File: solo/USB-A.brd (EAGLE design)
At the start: 42.8 x 15 mm, 23 parts, among them U1 USB_TRACES

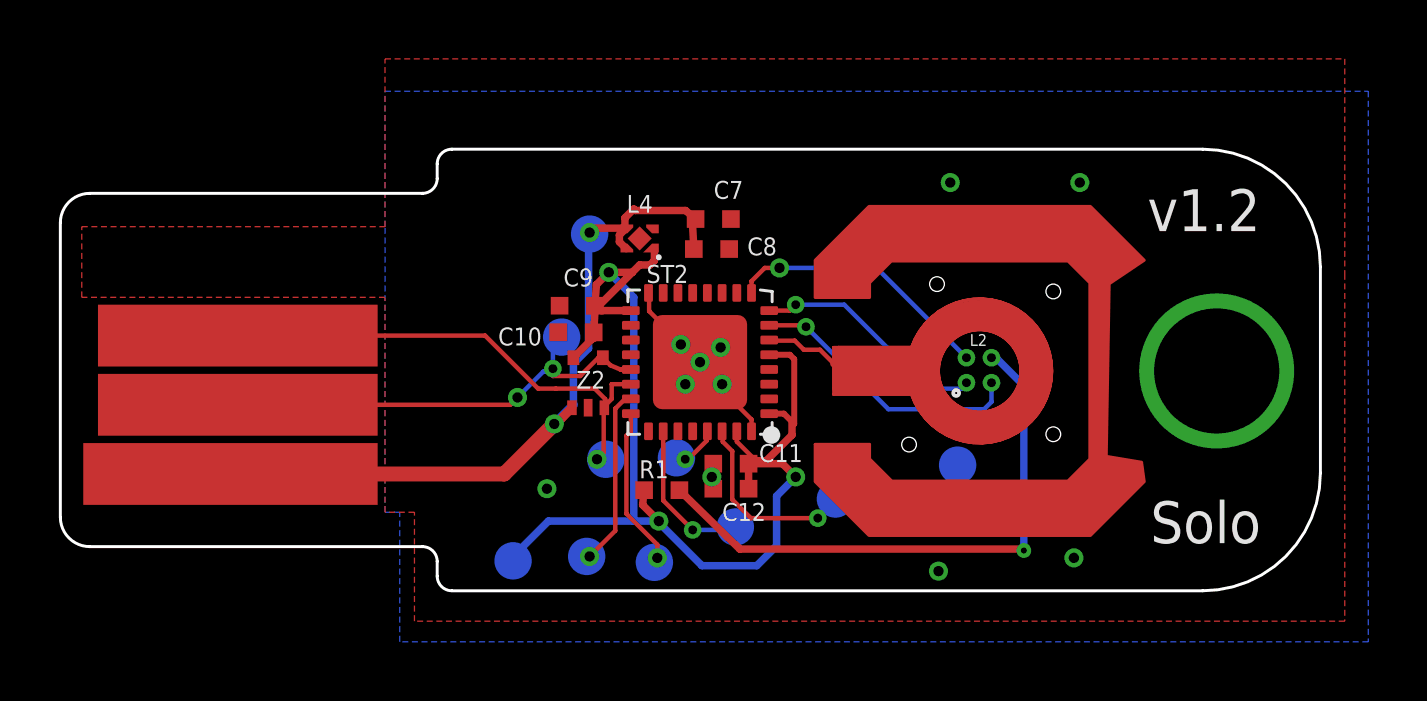
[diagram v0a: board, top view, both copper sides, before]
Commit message: fix AMS part footprint :(
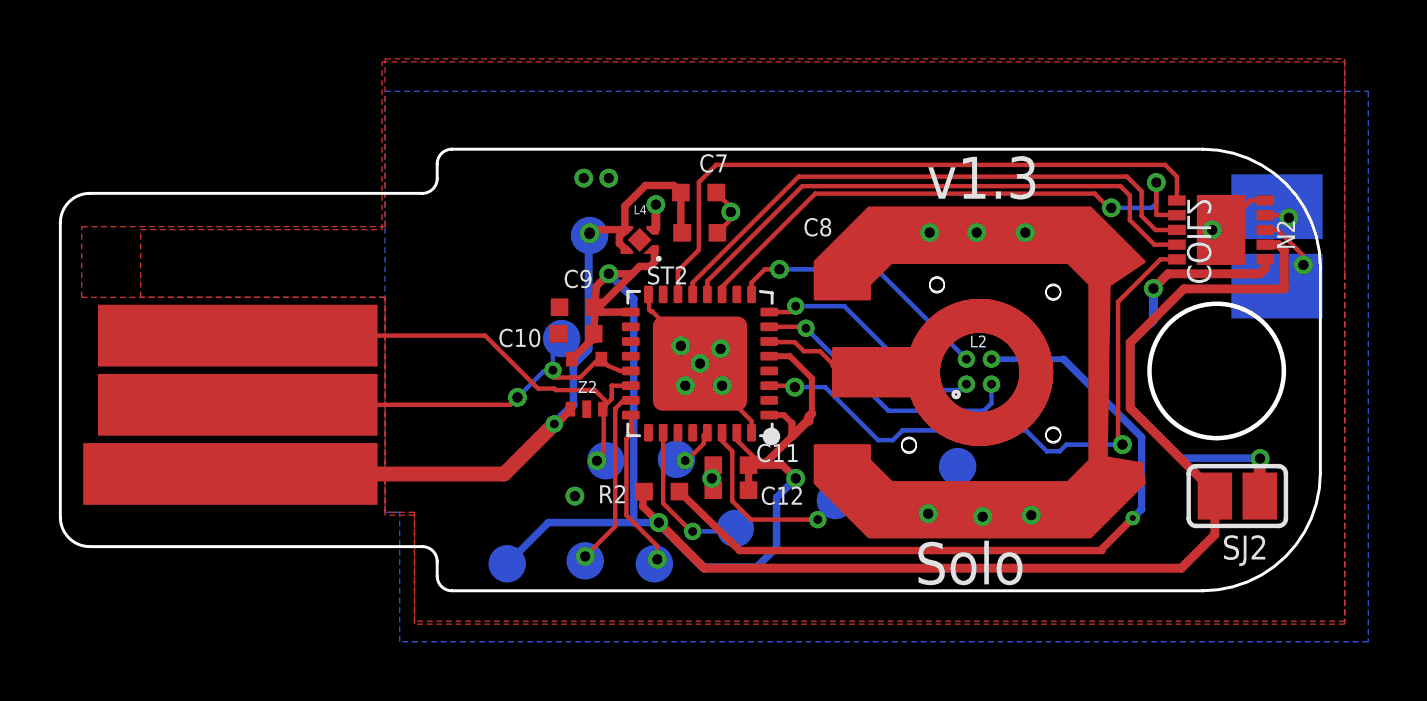
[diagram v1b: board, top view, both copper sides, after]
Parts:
- removed R1: 175, efm-fido:R0402
- added COIL2: MOLEX_NFC_COIL_1462360101, efm-fido:MOLEX_NFC_COIL1
- added N2: AMS3956, efm-fido:MLPD3X3
- added R2: 175, efm-fido:R0402
- added SJ2: (no value), jumper:SJ
- moved C7 1.03 mm to (54.9, 60.3)
- moved C8 0.68 mm to (54.9, 58.9)
- moved 3V1 0.22 mm to (48.4, 47.6)
- moved SWDIO1 0.16 mm to (51.0, 47.8)
- moved Z2 0.07 mm to (50.5, 52.9)
- moved +5V1 0.05 mm to (51.1, 58.8)
- moved C12 0.05 mm to (56.0, 50.1)
- moved D+1 0.05 mm to (51.7, 51.1)
- moved D-1 0.05 mm to (50.2, 55.3)
- moved L4 0.05 mm to (52.9, 58.6)
- moved SRX<-1 0.05 mm to (59.5, 49.8)
- moved SWCLK1 0.05 mm to (53.4, 47.6)
- moved U$2 0.05 mm to (64.4, 54.1)
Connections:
- removed net N$7: L2.P$4, R1.1
- new net AMS_CS: N2.P6, ST2.14
- new net AMS_IRQ: N2.P10, ST2.3
- new net MISO: N2.P9, ST2.12
- new net MOSI: N2.P8, ST2.13
- new net N$15: L2.P$4, R2.1
- new net N$23: N2.P1, SJ2.1
- new net N$25: COIL2.P$1, N2.P4
- new net N$26: COIL2.P$2, N2.P3
- new net SCLK: N2.P7, ST2.11
- net +3V3: now also N2.P2, R2.2, SJ2.2; no longer R1.2
- net PE: now also N2.P$11, N2.P5
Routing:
- net +3V3: track 42.4 -> 79.2 mm
- net N$15: track 0.00 -> 25.9 mm, vias 0 -> 2
- net AMS_CS: track 0.00 -> 21.6 mm
- net AMS_IRQ: track 0.00 -> 20.8 mm, vias 0 -> 2
- net N$7: track 19.7 -> 0.00 mm, vias 2 -> 0
- net MOSI: track 0.00 -> 19.6 mm
- net SCLK: track 0.00 -> 19.3 mm, vias 0 -> 2
- net MISO: track 0.00 -> 19.0 mm
- net N$23: track 0.00 -> 15.1 mm, vias 0 -> 2
- net PE: track 12.0 -> 16.9 mm, vias 11 -> 18
- net +5V: track 27.1 -> 31.6 mm, vias 2 -> 3
- net N$26: track 0.00 -> 3.28 mm, vias 0 -> 1
- net N$25: track 0.00 -> 1.51 mm, vias 0 -> 1
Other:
- outline, holes or cut-outs redrawn
- board text added: "v1.3"
- board text removed: "v1.2"
